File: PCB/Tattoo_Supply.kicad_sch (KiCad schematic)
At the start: 6 parts, among them J1 Barrel_Jack_Switch, J2 Out_{1}, J3 Out_{2}, Q1 SiA441DJ

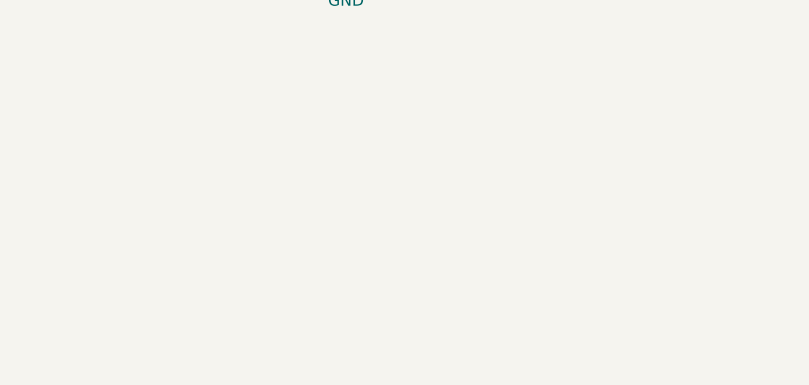
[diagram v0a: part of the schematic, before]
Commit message: add 3d models
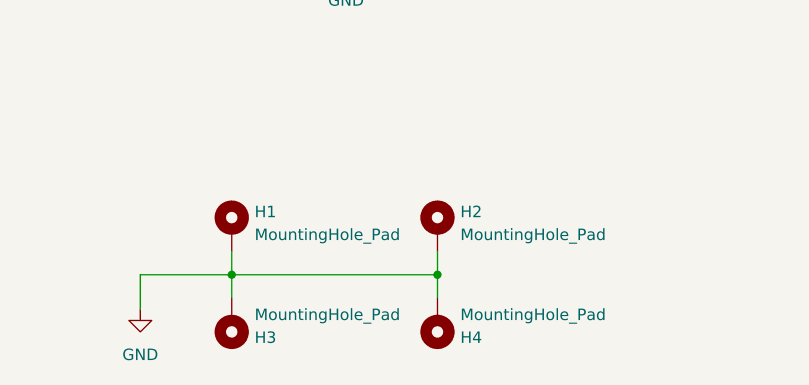
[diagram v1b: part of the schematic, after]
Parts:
- added H1, H2, H3, H4: MountingHole_Pad, MountingHole:MountingHole_2.7mm_M2.5_DIN965_Pad, symbol Mechanical:MountingHole_Pad
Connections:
- net GND: now also H1.1, H2.1, H3.1, H4.1
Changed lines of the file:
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@@
     (rev "V1.0")
   )
+  (bus_alias "UART" (members "Tx" "Rx"))
+  (bus_alias "I2C" (members "SDA" "SCL"))
   (bus_alias "SPI" (members "~{CS}" "SCK" "MOSI" "MISO"))
   (bus_alias "USB2" (members "D+" "D-"))
-  (bus_alias "I2C" (members "SDA" "SCL"))
-  (bus_alias "UART" (members "Tx" "Rx"))
   (bus_alias "Encoder" (members "DT" "CLK" "SW"))
   (junction (at 46.99 119.38) (diameter 0) (color 0 0 0 0)
@@
   (junction (at 60.96 124.46) (diameter 0) (color 0 0 0 0)
   )
+  (junction (at 48.26 171.45) (diameter 0) (color 0 0 0 0)
+  )
   (junction (at 69.85 114.3) (diameter 0) (color 0 0 0 0)
   )
+  (junction (at 71.12 171.45) (diameter 0) (color 0 0 0 0)
+  )
   (bus (pts (xy 168.91 139.7) (xy 207.01 139.7))
     (stroke (width 0) (type default))
   )
+  (wire (pts (xy 71.12 171.45) (xy 71.12 173.99))
+    (stroke (width 0) (type default))
+  )
   (wire (pts (xy 203.2 50.8) (xy 207.01 50.8))
     (stroke (width 0) (type default))
   )
+  (wire (pts (xy 48.26 171.45) (xy 48.26 173.99))
+    (stroke (width 0) (type default))
+  )
   (wire (pts (xy 54.61 74.93) (xy 63.5 74.93))
     (stroke (width 0) (type default))
@@
     (stroke (width 0) (type default))
   )
+  (wire (pts (xy 71.12 171.45) (xy 71.12 168.91))
+    (stroke (width 0) (type default))
+  )
   (wire (pts (xy 69.85 123.19) (xy 69.85 124.46))
     (stroke (width 0) (type default))
@@
     (stroke (width 0) (type default))
   )
+  (wire (pts (xy 48.26 171.45) (xy 71.12 171.45))
+    (stroke (width 0) (type default))
+  )
   (wire (pts (xy 222.25 82.55) (xy 226.06 82.55))
     (stroke (width 0) (type default))
@@
     (stroke (width 0) (type default))
   )
+  (wire (pts (xy 48.26 168.91) (xy 48.26 171.45))
+    (stroke (width 0) (type default))
+  )
   (wire (pts (xy 166.37 82.55) (xy 170.18 82.55))
     (stroke (width 0) (type default))
@@
     (stroke (width 0) (type default))
   )
+  (wire (pts (xy 38.1 171.45) (xy 48.26 171.45))
+    (stroke (width 0) (type default))
+  )
   (wire (pts (xy 156.21 107.95) (xy 156.21 111.76))
     (stroke (width 0) (type default))
@@
   )
   (wire (pts (xy 111.76 40.64) (xy 115.57 40.64))
+    (stroke (width 0) (type default))
+  )
+  (wire (pts (xy 38.1 175.26) (xy 38.1 171.45))
     (stroke (width 0) (type default))
   )
@@
         (path "/036b57f3-323c-4da7-bad2-1c27fa1415e1"
           (reference "#PWR03") (unit 1)
+        )
+      )
+    )
+  )
+  (symbol (lib_id "Mechanical:MountingHole_Pad") (at 48.26 166.37 0) (unit 1)
+    (in_bom no) (on_board yes) (dnp no) (fields_autoplaced)
+    (property "Reference" "H1" (at 50.8 164.465 0)
+      (effects (font (size 1.27 1.27)) (justify left))
+    )
+    (property "Value" "MountingHole_Pad" (at 50.8 167.005 0)
+      (effects (font (size 1.27 1.27)) (justify left))
+    )
+    (property "Footprint" "MountingHole:MountingHole_2.7mm_M2.5_DIN965_Pad" (at 48.26 166.37 0)
+      (effects (font (size 1.27 1.27)) hide)
+    )
+    (property "Datasheet" "~" (at 48.26 166.37 0)
+      (effects (font (size 1.27 1.27)) hide)
+    )
+    (pin "1")
+    (instances
+      (project "Tattoo_Supply"
+        (path "/036b57f3-323c-4da7-bad2-1c27fa1415e1"
+          (reference "H1") (unit 1)
         )
       )
@@
     )
   )
+  (symbol (lib_id "Mechanical:MountingHole_Pad") (at 71.12 176.53 0) (mirror x) (unit 1)
+    (in_bom no) (on_board yes) (dnp no) (fields_autoplaced)
+    (property "Reference" "H4" (at 73.66 178.435 0)
+      (effects (font (size 1.27 1.27)) (justify left))
+    )
+    (property "Value" "MountingHole_Pad" (at 73.66 175.895 0)
+      (effects (font (size 1.27 1.27)) (justify left))
+    )
+    (property "Footprint" "MountingHole:MountingHole_2.7mm_M2.5_DIN965_Pad" (at 71.12 176.53 0)
+      (effects (font (size 1.27 1.27)) hide)
+    )
+    (property "Datasheet" "~" (at 71.12 176.53 0)
+      (effects (font (size 1.27 1.27)) hide)
+    )
+    (pin "1")
+    (instances
+      (project "Tattoo_Supply"
+        (path "/036b57f3-323c-4da7-bad2-1c27fa1415e1"
+          (reference "H4") (unit 1)
+        )
+      )
+    )
+  )
   (symbol (lib_id "Device:D_Zener") (at 69.85 119.38 270) (unit 1)
     (in_bom yes) (on_board yes) (dnp no) (fields_autoplaced)
@@
         (path "/036b57f3-323c-4da7-bad2-1c27fa1415e1"
           (reference "#PWR08") (unit 1)
+        )
+      )
+    )
+  )
+  (symbol (lib_id "power:GND") (at 38.1 175.26 0) (unit 1)
+    (in_bom yes) (on_board yes) (dnp no) (fields_autoplaced)
+    (property "Reference" "#PWR079" (at 38.1 181.61 0)
+      (effects (font (size 1.27 1.27)) hide)
+    )
+    (property "Value" "GND" (at 38.1 180.34 0)
+      (effects (font (size 1.27 1.27)))
+    )
+    (property "Footprint" "" (at 38.1 175.26 0)
+      (effects (font (size 1.27 1.27)) hide)
+    )
+    (property "Datasheet" "" (at 38.1 175.26 0)
+      (effects (font (size 1.27 1.27)) hide)
+    )
+    (pin "1")
+    (instances
+      (project "Tattoo_Supply"
+        (path "/036b57f3-323c-4da7-bad2-1c27fa1415e1"
+          (reference "#PWR079") (unit 1)
         )
       )
@@
     )
   )
+  (symbol (lib_id "Mechanical:MountingHole_Pad") (at 71.12 166.37 0) (unit 1)
+    (in_bom no) (on_board yes) (dnp no) (fields_autoplaced)
+    (property "Reference" "H2" (at 73.66 164.465 0)
+      (effects (font (size 1.27 1.27)) (justify left))
+    )
+    (property "Value" "MountingHole_Pad" (at 73.66 167.005 0)
+      (effects (font (size 1.27 1.27)) (justify left))
+    )
+    (property "Footprint" "MountingHole:MountingHole_2.7mm_M2.5_DIN965_Pad" (at 71.12 166.37 0)
+      (effects (font (size 1.27 1.27)) hide)
+    )
+    (property "Datasheet" "~" (at 71.12 166.37 0)
+      (effects (font (size 1.27 1.27)) hide)
+    )
+    (pin "1")
+    (instances
+      (project "Tattoo_Supply"
+        (path "/036b57f3-323c-4da7-bad2-1c27fa1415e1"
+          (reference "H2") (unit 1)
+        )
+      )
+    )
+  )
   (symbol (lib_id "power:+3V3") (at 215.9 118.11 0) (unit 1)
     (in_bom yes) (on_board yes) (dnp no) (fields_autoplaced)
@@
         )
       )
+    )
+  )
+  (symbol (lib_id "Mechanical:MountingHole_Pad") (at 48.26 176.53 0) (mirror x) (unit 1)
+    (in_bom no) (on_board yes) (dnp no) (fields_autoplaced)
+    (property "Reference" "H3" (at 50.8 178.435 0)
+      (effects (font (size 1.27 1.27)) (justify left))
+    )
+    (property "Value" "MountingHole_Pad" (at 50.8 175.895 0)
+      (effects (font (size 1.27 1.27)) (justify left))
+    )
+    (property "Footprint" "MountingHole:MountingHole_2.7mm_M2.5_DIN965_Pad" (at 48.26 176.53 0)
+      (effects (font (size 1.27 1.27)) hide)
+    )
+    (property "Datasheet" "~" (at 48.26 176.53 0)
+      (effects (font (size 1.27 1.27)) hide)
+    )
+    (pin "1")
+    (instances
+      (project "Tattoo_Supply"
+        (path "/036b57f3-323c-4da7-bad2-1c27fa1415e1"
+          (reference "H3") (unit 1)
+        )
+      )

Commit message: Release V1.0
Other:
- company: (none) -> axoulc
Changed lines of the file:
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@@
   (title_block
     (title "Tattoo Power Supply")
+    (date "2023-03-13")
     (rev "V1.0")
+    (company "axoulc")
   )
-  (bus_alias "I2C" (members "SDA" "SCL"))
-  (bus_alias "UART" (members "Tx" "Rx"))
-  (bus_alias "USB2" (members "D+" "D-"))
   (bus_alias "Encoder" (members "DT" "CLK" "SW"))
   (bus_alias "SPI" (members "~{CS}" "SCK" "MOSI" "MISO"))
+  (bus_alias "I2C" (members "SDA" "SCL"))
+  (bus_alias "USB2" (members "D+" "D-"))
+  (bus_alias "UART" (members "Tx" "Rx"))
   (junction (at 46.99 119.38) (diameter 0) (color 0 0 0 0)
   )
